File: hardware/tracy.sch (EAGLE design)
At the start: 76 parts, among them IC1 SIM900, J1 U.FL, J2 U.FL, Q4 si2305cd, T1 BC846, T2 BC846, U1 SPX5205 3v3, U2 3339, U3 TC1014 2V8, Y1 32768Hz CFPX-217 12.5pF

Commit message: foo
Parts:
- D1: value DIODE-SCHOTTKY_ -> 15MQ040N
- X1: value prog -> MOLEX_6VERTICAL
- renumbered U$20 to X1
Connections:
- net GPRS_EN renamed GPRS_VBAT
- net GPRS_POW renamed GPRS_PWRKEY
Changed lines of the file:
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@@
 <part name="U$2" library="Simplex-rlc" deviceset="RES_ARR" device="" value="470"/>
 <part name="+3V2" library="supply1" deviceset="+3V3" device=""/>
-<part name="D1" library="SparkFun-DiscreteSemi" deviceset="DIODE-SCHOTTKY" device="_"/>
+<part name="D1" library="SparkFun-DiscreteSemi" deviceset="DIODE-SCHOTTKY" device="_" value="15MQ040N"/>
 <part name="R3" library="rcl" deviceset="R-EU_" device="R0805W" value="2M"/>
 <part name="R4" library="rcl" deviceset="R-EU_" device="R0805W" value="1M3"/>
@@
 <part name="U$17" library="Simplex-Connectors" deviceset="MOLEX_4" device="HORIZONTAL" value="5V"/>
 <part name="U$19" library="Simplex-Connectors" deviceset="MOLEX_4" device="HORIZONTAL" value="LiPo"/>
-<part name="U$20" library="Simplex-Connectors" deviceset="MOLEX_6" device="VERTICAL" value="prog"/>
 <part name="R6" library="rcl" deviceset="R-EU_" device="R0805W" value="100k"/>
 <part name="GND36" library="SparkFun" deviceset="GND" device=""/>
@@
 <part name="T1" library="transistor" deviceset="BC846" device=""/>
 <part name="GND58" library="SparkFun" deviceset="GND" device=""/>
+<part name="X1" library="Simplex-Connectors" deviceset="MOLEX_6" device="VERTICAL"/>
 </parts>
 <sheets>
@@
 <instance part="U$17" gate="G$1" x="231.14" y="25.4"/>
 <instance part="U$19" gate="G$1" x="259.08" y="33.02" rot="MR180"/>
-<instance part="U$20" gate="G$1" x="195.58" y="27.94"/>
 <instance part="R6" gate="G$1" x="111.76" y="93.98" rot="R270"/>
 <instance part="GND36" gate="1" x="111.76" y="83.82"/>
@@
 <instance part="T1" gate="G$1" x="223.52" y="243.84"/>
 <instance part="GND58" gate="1" x="226.06" y="231.14"/>
+<instance part="X1" gate="G$1" x="195.58" y="27.94"/>
 </instances>
 <busses>
@@
 <segment>
 <wire x1="193.04" y1="33.02" x2="190.5" y2="33.02" width="0.1524" layer="91"/>
-<pinref part="U$20" gate="G$1" pin="1"/>
 <pinref part="GND27" gate="1" pin="GND"/>
 <wire x1="190.5" y1="33.02" x2="190.5" y2="15.24" width="0.1524" layer="91"/>
+<pinref part="X1" gate="G$1" pin="1"/>
 </segment>
 </net>
@@
 <wire x1="193.04" y1="20.32" x2="182.88" y2="20.32" width="0.1524" layer="91"/>
 <label x="182.88" y="20.32" size="1.778" layer="95"/>
-<pinref part="U$20" gate="G$1" pin="6"/>
+<pinref part="X1" gate="G$1" pin="6"/>
 </segment>
 </net>
@@
 <pinref part="R34" gate="G$1" pin="1"/>
 <wire x1="175.26" y1="30.48" x2="193.04" y2="30.48" width="0.1524" layer="91"/>
-<pinref part="U$20" gate="G$1" pin="2"/>
+<pinref part="X1" gate="G$1" pin="2"/>
 </segment>
 </net>
@@
 <label x="182.88" y="27.94" size="1.778" layer="95"/>
 <pinref part="R35" gate="G$1" pin="1"/>
-<pinref part="U$20" gate="G$1" pin="3"/>
+<pinref part="X1" gate="G$1" pin="3"/>
 </segment>
 </net>
@@
 <wire x1="193.04" y1="22.86" x2="182.88" y2="22.86" width="0.1524" layer="91"/>
 <label x="182.88" y="22.86" size="1.778" layer="95"/>
-<pinref part="U$20" gate="G$1" pin="5"/>
+<pinref part="X1" gate="G$1" pin="5"/>
 </segment>
 </net>
@@
 </segment>
 </net>
-<net name="GPRS_POW" class="0">
+<net name="GPRS_PWRKEY" class="0">
 <segment>
 <pinref part="R20" gate="G$1" pin="2"/>
@@
 </segment>
 </net>
-<net name="GPRS_EN" class="0">
+<net name="GPRS_VBAT" class="0">
 <segment>
 <pinref part="R23" gate="G$1" pin="1"/>
@@
 <label x="182.88" y="25.4" size="1.778" layer="95"/>
 <pinref part="U$12" gate="G$1" pin="2V8"/>
-<pinref part="U$20" gate="G$1" pin="4"/>
-</segment>
-<segment>
+<pinref part="X1" gate="G$1" pin="4"/>
+</segment>
+<segment>

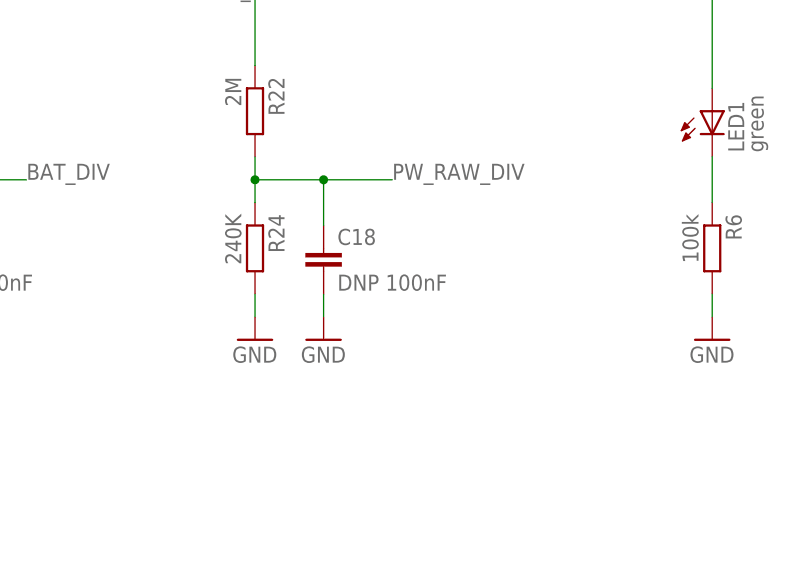
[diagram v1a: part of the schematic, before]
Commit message: keepout under fuse
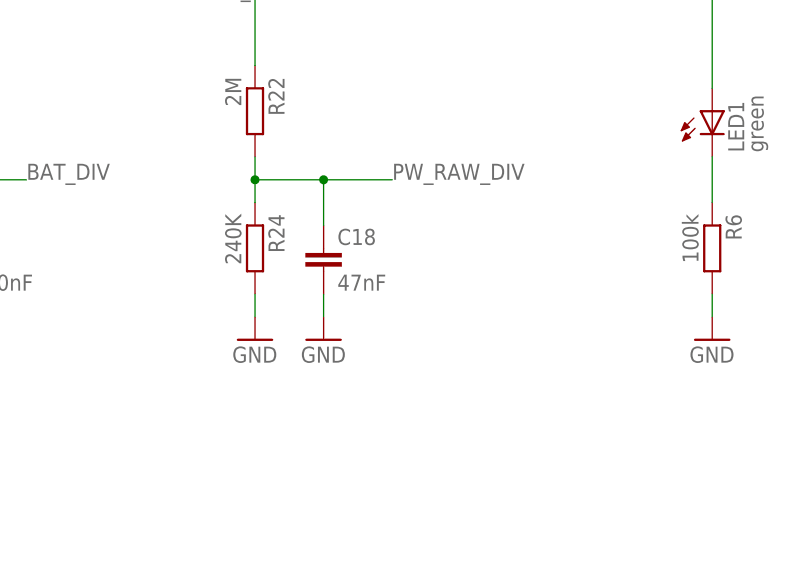
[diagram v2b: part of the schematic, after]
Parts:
- C18: value DNP 100nF -> 47nF
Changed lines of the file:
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@@
 <part name="C9" library="rcl" deviceset="C-EU" device="C0805" value="100nF"/>
 <part name="GND10" library="SparkFun" deviceset="GND" device=""/>
-<part name="C18" library="rcl" deviceset="C-EU" device="C0805" value="DNP 100nF"/>
+<part name="C18" library="rcl" deviceset="C-EU" device="C0805" value="47nF"/>
 <part name="GND38" library="SparkFun" deviceset="GND" device=""/>
 <part name="GND39" library="SparkFun" deviceset="GND" device=""/>

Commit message: add fram buffer
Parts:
- removed R8: 330, rcl:R-EU_R0805W
- added C19: 100nF, rcl:C-EUC0805
- added R2: 6K2, rcl:R-EU_R0805W
- added X2: MOLEX_2HORIZONTAL, Simplex-Connectors:MOLEX_2HORIZONTAL
- R5: value 1k -> 4k7
- U$17: value 5V -> FM24V; device Simplex-Connectors:MOLEX_4HORIZONTAL -> Simplex-ICs:FM24V
- U$9: value RESETTABLE -> RESETTABLE_0805; device Simplex-Fuses:RESETTABLE -> Simplex-Fuses:RESETTABLE_0805
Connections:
- net PW_RAW_DIV renamed 5V_DIV
- removed net GPS_BKP: R8.2, U$1.35
- removed net N$11: C11.1, R1.2, R8.1, U2.VBACKUP
- removed net N$12: R5.1, U$17.2
- removed net N$31: R1.1, U2.NRESET
- removed net PW_EN: R5.2, U$1.36
- removed net PW_RAW: R22.1, U$17.1
- new net SCL_FM: R1.1, U$1.35, U$17.SCL
- new net SDA_FM: R5.1, U$1.36, U$17.SDA
- net 2V8: now also C11.1, C19.1, R1.2, R5.2, U$17.VCC, U2.VBACKUP
- net 5V: now also X2.2; no longer U$17.4
- net 5V_IN: now also R22.1
- net GND: now also C19.2, R2.1, U$17.A1, U$17.A2, U$17.GND, X2.1; no longer U$17.3
- net N$3: now also R2.2
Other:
- note added: "1.1"
- note removed: "01"
- moved on the sheet: C5, C7, R1, R34, R35, R5, U$19, U$2, U$5, X1

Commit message: rev 2
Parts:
- removed R17: 10k, rcl:R-EU_R0805W
- removed U$19: LiPo, Simplex-Connectors:MOLEX_4HORIZONTAL
- added R7, R8: 4k7, rcl:R-EU_R0805W
- added X3: MOLEX_6HORIZONTAL, Simplex-Connectors:MOLEX_6HORIZONTAL
- added X4: MOLEX_2HORIZONTAL, Simplex-Connectors:MOLEX_2HORIZONTAL
- C11: value 10uF -> 1uF
- C3: device rcl:C-EUC1206 -> rcl:C-EUC0805
- U$3: value SIMLOCKC707_10M006_000_2 -> SIM_MOLEX_7880-0001; device Simplex-Connectors:SIMLOCKC707_10M006_000_2 -> Simplex-Connectors:SIM_MOLEX_7880-0001
- X1: value MOLEX_6VERTICAL -> MOLEX_2HORIZONTAL; device Simplex-Connectors:MOLEX_6VERTICAL -> Simplex-Connectors:MOLEX_2HORIZONTAL
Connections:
- removed net N$42: IC1G$1.SIM_PRESENCE, R17.2, U$3.LOCK_01, U$8.CATODE1
- removed net N$43: IC1G$1.VDD_EXT, R17.1
- net 2V8: now also R7.1, R8.1, X3.4; no longer X1.4
- net 5V: now also X1.1; no longer X2.2
- net BAT: now also X2.1; no longer U$19.1
- net GND: now also U$3.SH@1, U$3.SH@2, U$3.SH@3, U$3.SH@4, X1.2, X2.2, X3.1, X4.1; no longer U$19.2, U$19.3, U$3.LOCK_02, X1.1, X2.1
- net P4.0: now also R8.2, X3.5; no longer X1.5
- net P4.1: now also R7.2, X3.6; no longer X1.6
- net RST: now also X3.2; no longer X1.2
- net TEST: now also X3.3; no longer X1.3
- net TS: now also X4.2; no longer U$19.4
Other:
- moved on the sheet: X2

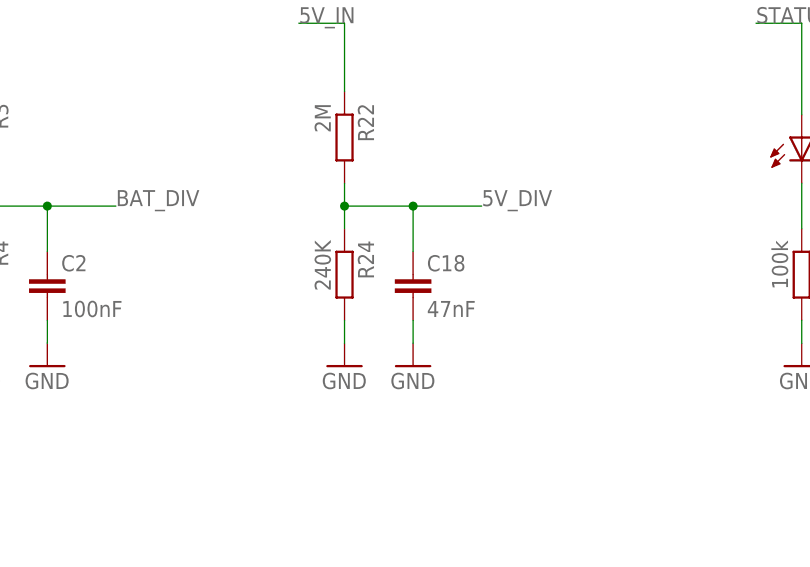
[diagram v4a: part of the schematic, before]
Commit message: move silkscreen labels
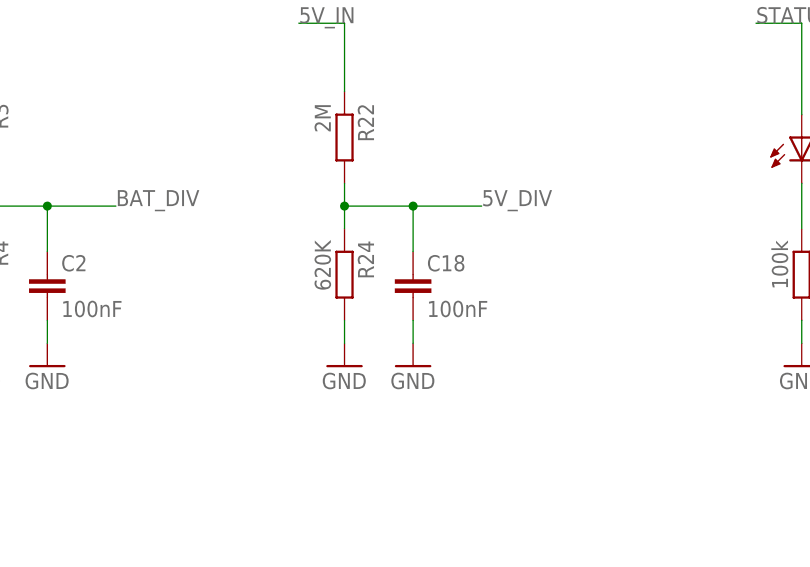
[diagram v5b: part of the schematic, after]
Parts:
- C18: value 47nF -> 100nF
- R24: value 240K -> 620K
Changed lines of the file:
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@@
 <part name="GND47" library="SparkFun" deviceset="GND" device=""/>
 <part name="R22" library="rcl" deviceset="R-EU_" device="R0805W" value="2M"/>
-<part name="R24" library="rcl" deviceset="R-EU_" device="R0805W" value="240K"/>
+<part name="R24" library="rcl" deviceset="R-EU_" device="R0805W" value="620K"/>
 <part name="GND34" library="SparkFun" deviceset="GND" device=""/>
 <part name="GND27" library="SparkFun" deviceset="GND" device=""/>
@@
 <part name="C9" library="rcl" deviceset="C-EU" device="C0805" value="100nF"/>
 <part name="GND10" library="SparkFun" deviceset="GND" device=""/>
-<part name="C18" library="rcl" deviceset="C-EU" device="C0805" value="47nF"/>
+<part name="C18" library="rcl" deviceset="C-EU" device="C0805" value="100nF"/>
 <part name="GND38" library="SparkFun" deviceset="GND" device=""/>
 <part name="GND39" library="SparkFun" deviceset="GND" device=""/>

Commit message: manual update
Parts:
- C13: value 100n -> 100nF
- C14: value 22p -> 22pF
- U$1: value F55[0/1]X---PT48 -> MSP430F5510
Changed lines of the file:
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@@
 <part name="FRAME1" library="frames" deviceset="DOCFIELD" device="" value="ihaaa"/>
 <part name="U$7" library="SparkFun" deviceset="OSHW-LOGO" device="M"/>
-<part name="U$1" library="TI_MSP430_v16" deviceset="F55[0/1]X---PT48" device=""/>
+<part name="U$1" library="TI_MSP430_v16" deviceset="F55[0/1]X---PT48" device="" value="MSP430F5510"/>
 <part name="GND16" library="SparkFun" deviceset="GND" device=""/>
 <part name="GND22" library="SparkFun" deviceset="GND" device=""/>
@@
 <part name="GND28" library="SparkFun" deviceset="GND" device=""/>
 <part name="GND29" library="SparkFun" deviceset="GND" device=""/>
-<part name="C13" library="rcl" deviceset="C-EU" device="C0805" value="100n"/>
+<part name="C13" library="rcl" deviceset="C-EU" device="C0805" value="100nF"/>
 <part name="GND31" library="SparkFun" deviceset="GND" device=""/>
-<part name="C14" library="rcl" deviceset="C-EU" device="C0805" value="22p"/>
+<part name="C14" library="rcl" deviceset="C-EU" device="C0805" value="22pF"/>
 <part name="GND37" library="SparkFun" deviceset="GND" device=""/>
 <part name="T2" library="transistor" deviceset="BC846" device=""/>

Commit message: latest
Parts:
- added C22: 100nF, rcl:C-EUC0805
- added JP1: no_prot, SparkFun-Passives:JUMPER-2SMD-NO
- added Q1: si2305cd, Simplex-DiscreteSemi:MOSFET-PCHANNELSMD_POWER
- added R9: 4k7, rcl:R-EU_R0805W
- added TP1, TP101, TP102, TP103: TPTP12R, testpad:TPTP12R
- D1: value 15MQ040N -> bzm55c5v6; device SparkFun-DiscreteSemi:DIODE-SCHOTTKY_ -> diode:DIODE-MICROMELF-W
- R21: value 10k -> 100k
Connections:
- net CH renamed CHG
- removed net N$20: D1.A, U$9.P$2
- new net N$11: D1.A, Q1.G, R9.1
- new net N$5: JP1.1, Q1.D, U$9.P$2
- net +3V3: now also TP103.TP; no longer TP3.TP
- net 2V8: now also TP102.TP; no longer TP2.TP
- net 5V_IN: now also JP1.2, Q1.S
- net GND: now also R9.2, TP1.TP, TP101.TP; no longer TP4.TP, TP5.TP, TP6.TP
- net GPRS_RX: now also TP4.TP
- net GPS_RX: now also TP2.TP
- net GPS_TX: now also TP3.TP
- net N$10: now also TP5.TP
- net N$48: now also C22.2
- net N$49: now also C22.1
- net STATUS: now also TP6.TP
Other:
- note added: "2.1"
- note removed: "1.1"
- moved on the sheet: C1, C10, C11, C12, C13, C14, C15, C16, C17, C18, C19, C2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

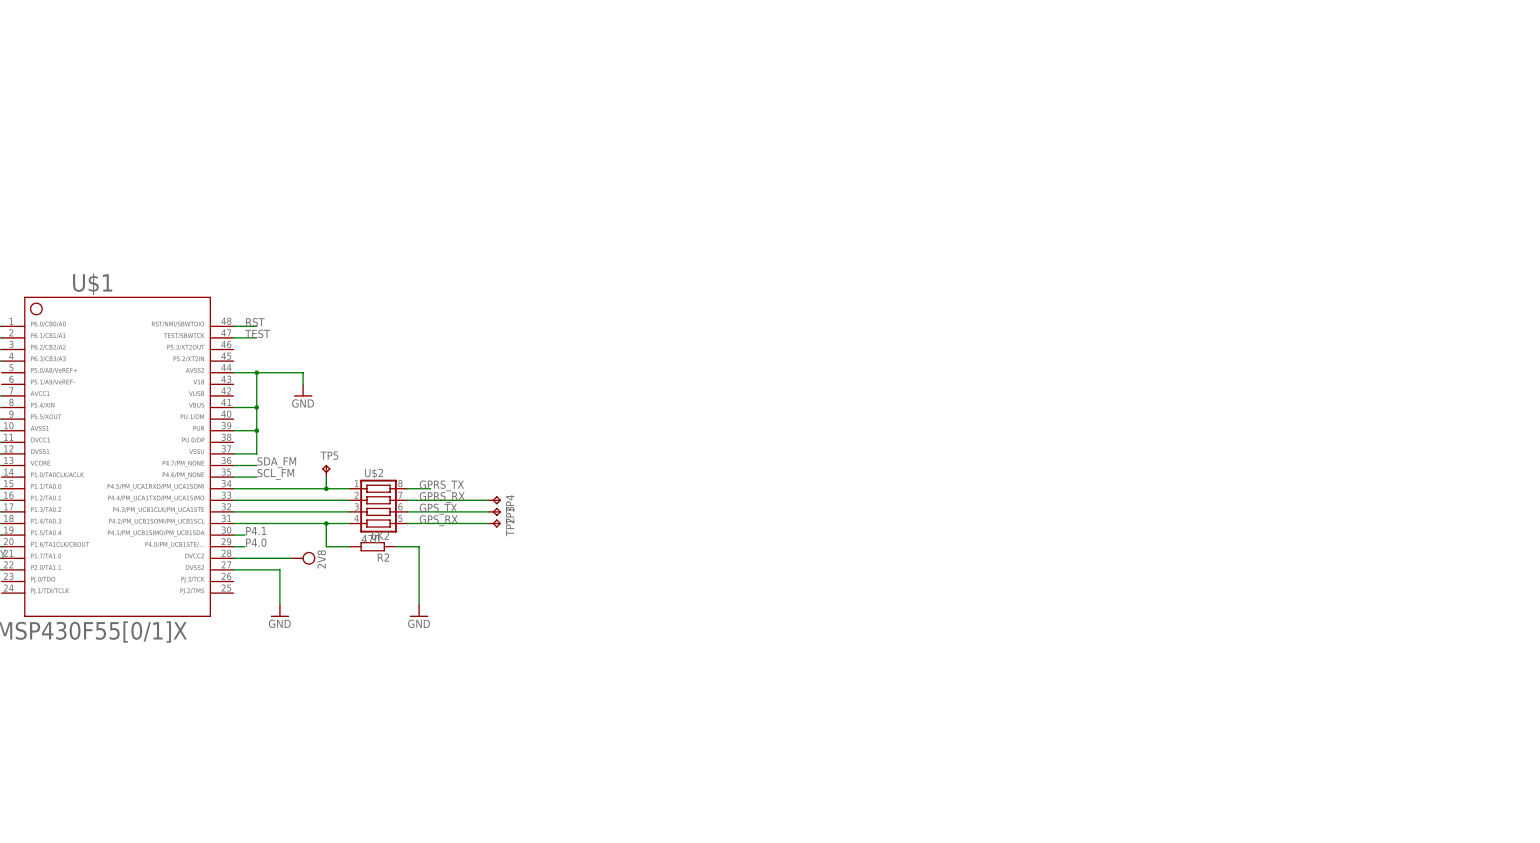
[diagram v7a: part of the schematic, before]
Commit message: rev3 - initial switch to msp430fr5994
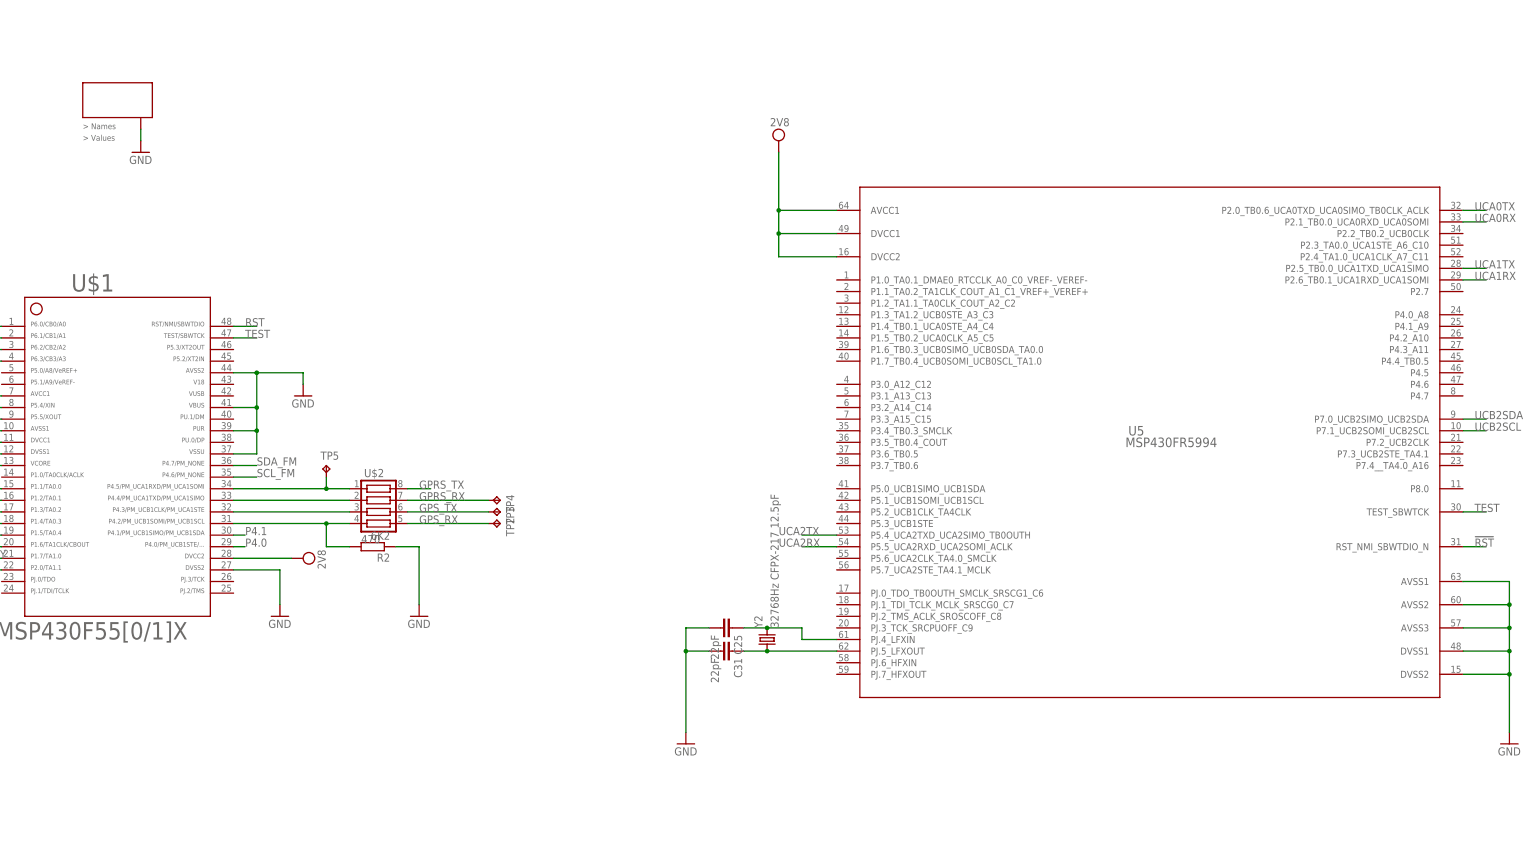
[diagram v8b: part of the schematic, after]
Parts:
- added C25, C31: 22pF, rcl:C-EUC0805
- added U$23: G203C, Simplex-Enclosures:G203C
- added U5: MSP430FR5994, Simplex-ICs:MSP430FR59941IPMR
- added Y2: 32768Hz CFPX-217 12.5pF, Simplex-FreqCtrl:CRYSTAL3.2X1.5
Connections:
- new net !RST: U5.RST_NMI_SBWTDIO_N
- new net N$12: C31.1, U5.PJ.5_LFXOUT, Y2.1
- new net N$13: C25.1, U5.PJ.4_LFXIN, Y2.2
- new net UCA0RX: U5.P2.1_TB0.0_UCA0RXD_UCA0SOMI
- new net UCA0TX: U5.P2.0_TB0.6_UCA0TXD_UCA0SIMO_TB0CLK_ACLK
- new net UCA1RX: U5.P2.6_TB0.1_UCA1RXD_UCA1SOMI
- new net UCA1TX: U5.P2.5_TB0.0_UCA1TXD_UCA1SIMO
- new net UCA2RX: U5.P5.5_UCA2RXD_UCA2SOMI_ACLK
- new net UCA2TX: U5.P5.4_UCA2TXD_UCA2SIMO_TB0OUTH
- new net UCB2SCL: U5.P7.1_UCB2SOMI_UCB2SCL
- new net UCB2SDA: U5.P7.0_UCB2SIMO_UCB2SDA
- net 2V8: now also U5.AVCC1, U5.DVCC1, U5.DVCC2
- net GND: now also C25.2, C31.2, U$23.SH, U5.AVSS1, U5.AVSS2, U5.AVSS3, U5.DVSS1, U5.DVSS2
- net TEST: now also U5.TEST_SBWTCK
